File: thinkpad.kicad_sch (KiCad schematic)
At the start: 130 parts, among them J1 Conn_01x06_MountingPin, J2 Conn_01x20_Socket, J3 Conn_01x06_Socket, J4 Touchpad_Conn, J5 Alt_USB, U1 Raspberry_Pi_Pico

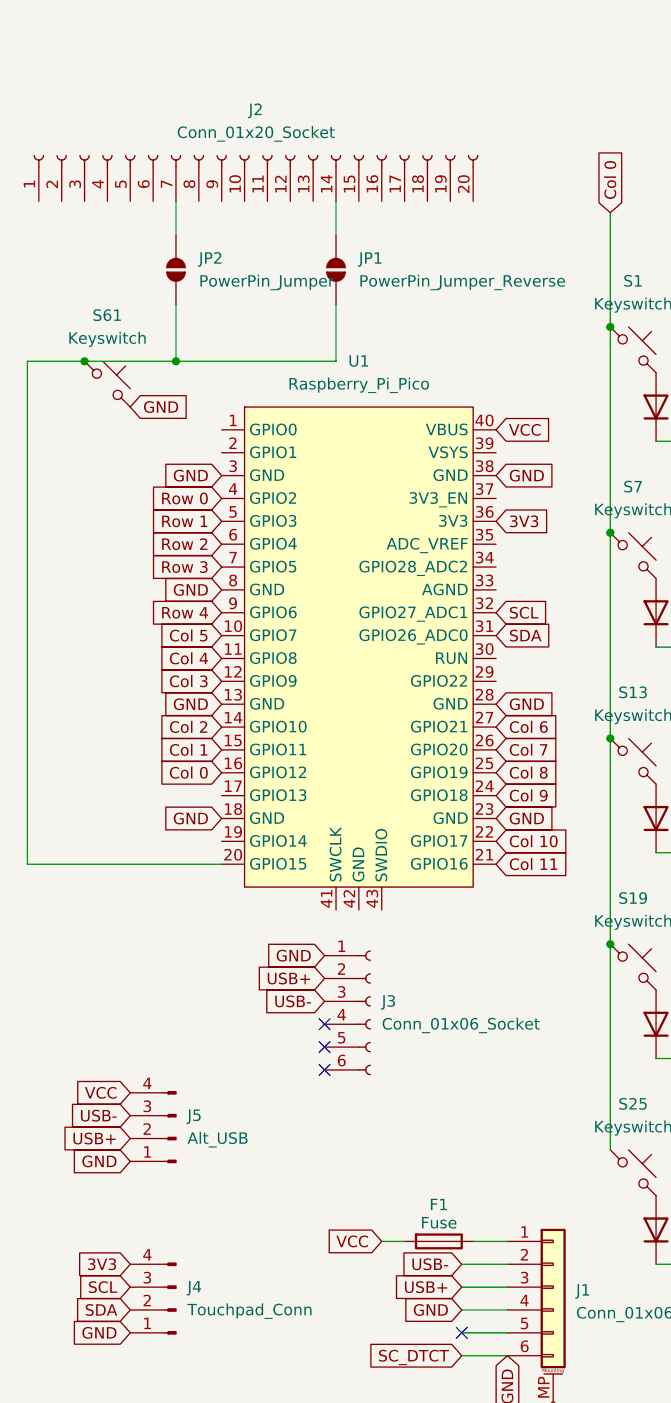
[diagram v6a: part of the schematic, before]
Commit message: filled zones set to no-island, vias added to make ground fills appear in more places (mostly aesthetic), keeb connector duuplicated, drc clean, unconnected 0, life is good
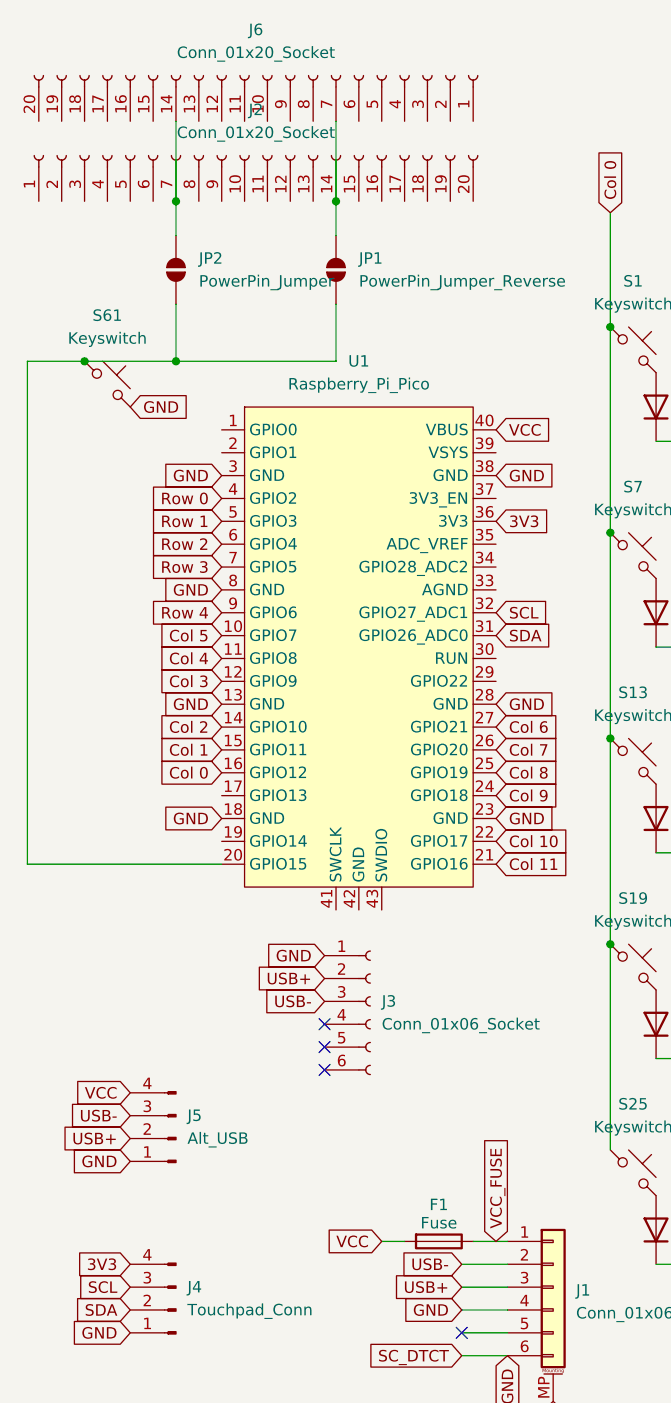
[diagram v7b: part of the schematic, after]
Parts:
- added J6: Conn_01x20_Socket, thinkpad-keyboard:Thinkpad-keyboard-fpc, symbol Connector:Conn_01x20_Socket
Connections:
- net at J2.7 (Pin_7), JP2.2 (B): now also J6.14 (Pin_14)
- net VCC_FUSE: now reaches F1.1, J1.1 (Pin_1)
- net at J2.14 (Pin_14), JP1.2 (B): now also J6.7 (Pin_7)
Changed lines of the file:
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@@
 	)
 	(junction
+		(at 52.07 25.4)
+		(diameter 0)
+		(color 0 0 0 0)
+	)
+	(junction
 		(at 139.7 107.95)
 		(diameter 0)
@@
 	)
 	(junction
+		(at 34.29 25.4)
+		(diameter 0)
+		(color 0 0 0 0)
+	)
+	(junction
 		(at 24.13 43.18)
 		(diameter 0)
@@
 	(wire
 		(pts
+			(xy 52.07 16.51) (xy 52.07 25.4)
+		)
+		(stroke
+			(width 0)
+			(type default)
+		)
+	)
+	(wire
+		(pts
 			(xy 128.27 39.37) (xy 128.27 62.23)
 		)
@@
 	(wire
 		(pts
+			(xy 34.29 16.51) (xy 34.29 25.4)
+		)
+		(stroke
+			(width 0)
+			(type default)
+		)
+	)
+	(wire
+		(pts
 			(xy 234.95 85.09) (xy 234.95 107.95)
 		)
@@
 		)
 	)
+	(global_label "VCC_FUSE"
+		(shape input)
+		(at 69.85 140.97 90)
+		(fields_autoplaced yes)
+		(effects
+			(font
+				(size 1.27 1.27)
+			)
+			(justify left)
+		)
+		(property "Intersheetrefs" "${INTERSHEET_REFS}"
+			(at 69.85 128.611 90)
+			(effects
+				(font
+					(size 1.27 1.27)
+				)
+				(justify left)
+				(hide yes)
+			)
+		)
+	)
 	(global_label "Col 11"
 		(shape input)
@@
 					(unit 1)
 				)
+			)
+		)
+	)
+	(symbol
+		(lib_id "Connector:Conn_01x20_Socket")
+		(at 44.45 11.43 270)
+		(mirror x)
+		(unit 1)
+		(exclude_from_sim no)
+		(in_bom yes)
+		(on_board yes)
+		(dnp no)
+		(property "Reference" "J6"
+			(at 43.18 6.35 90)
+			(effects
+				(font
+					(size 1.27 1.27)
+				)
+			)
+		)
+		(property "Value" "Conn_01x20_Socket"
+			(at 43.18 8.89 90)
+			(effects
+				(font
+					(size 1.27 1.27)
+				)
+			)
+		)
+		(property "Footprint" "thinkpad-keyboard:Thinkpad-keyboard-fpc"
+			(at 44.45 11.43 0)
+			(effects
+				(font
+					(size 1.27 1.27)
+				)
+				(hide yes)
+			)
+		)
+		(property "Datasheet" "~"
+			(at 44.45 11.43 0)
+			(effects
+				(font
+					(size 1.27 1.27)
+				)
+				(hide yes)
+			)
+		)
+		(property "Description" ""
+			(at 44.45 11.43 0)
+			(effects
+				(font
+					(size 1.27 1.27)
+				)
+				(hide yes)
+			)
+		)
+		(pin "1"
+		)
+		(pin "10"
+		)
+		(pin "11"
+		)
+		(pin "12"
+		)
+		(pin "13"
+		)
+		(pin "14"
+		)
+		(pin "15"
+		)
+		(pin "16"
+		)
+		(pin "17"
+		)
+		(pin "18"
+		)
+		(pin "19"
+		)
+		(pin "2"
+		)
+		(pin "20"
+		)
+		(pin "3"
+		)
+		(pin "4"
+		)
+		(pin "5"
+		)
+		(pin "6"
+		)
+		(pin "7"
+		)
+		(pin "8"
+		)
+		(pin "9"
+		)
+		(instances
+			(project "thinkpad"
+				(path "/5a75688f-62eb-4176-abdf-687d4570a106"
+					(reference "J6")
+					(unit 1)
+				)
